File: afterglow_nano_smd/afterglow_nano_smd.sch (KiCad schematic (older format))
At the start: 106 parts, among them J1 J137_IN_C, J2 J133_IN_R, J3 Conn_Power, J4 J133_OUT_R, J5 J137_OUT_C, J6 J134_OUT_R, J7 J138_OUT_C, J8 J135_OUT_R, J9 136_OUT_C, Q1 IRF5305, Q10 IRL2905, Q11 IRL2905, Q12 IRL2905, Q13 IRL2905, Q14 IRL2905, Q15 IRL2905, Q16 IRL2905, Q2 IRF5305, Q3 IRF5305, Q4 IRF5305, Q5 IRF5305, Q6 IRF5305, Q7 IRF5305, Q8 IRF5305, Q9 IRL2905, SW1 CFG, U1 74LS165, U2 74LS165, U3 5V_Regulator, U4 arduino_nano, U5 74HC595, U6 74HC595, U7 ULN2803A

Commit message: Converting...
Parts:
- removed D2: LED, LEDs:LED_0805_HandSoldering, symbol LED
- removed R26: 220, Resistors_SMD:R_0805_HandSoldering, symbol R
- removed SW1: CFG, Buttons_Switches_THT:SW_DIP_x4_W7.62mm_Slide, symbol SW_DIP_x04
- removed U4: arduino_nano, arduino_nano:arduino_mini, symbol arduino_nano
- added A1: Arduino_Nano_v3.x, Module:Arduino_Nano, symbol MCU_Module:Arduino_Nano_v3.x
- C1: symbol CP -> Device:CP
- C2, C3: symbol C_Small -> Device:C_Small
- C4: symbol C_Small -> afterglow_nano_smd-rescue:C_Small
- D1: symbol D -> Device:D
- F1: symbol Fuse -> Device:Fuse
- J1, J2, J4, J5, J6, J7, J8: symbol Conn_01x09_Male -> Connector:Conn_01x09_Male
- J3: symbol Conn_01x02 -> afterglow_nano_smd-rescue:Conn_01x02
- J9: symbol Conn_01x03_Male -> Connector:Conn_01x03_Male
- Q1, Q2, Q3, Q4, Q5, Q6, Q7, Q8: symbol IRF9540N -> afterglow_nano_smd-rescue:IRF9540N
- Q10, Q11, Q12, Q13, Q14, Q15, Q16, Q9: symbol IRF540N -> afterglow_nano_smd-rescue:IRF540N
- R1, R10, R11, R12, R13, R14, R15, R16, R18, R19, R2, R20, R21, R22, R23, R24, R27, R28, R29, R3, R30, R31, R32, R35, R36, R37, R38, R39, R4, R5, R6, R7, R8, R9: symbol R -> Device:R
- R17, R25, R33, R34, R40, R41, R42, R43, R44, R45, R46, R47, R48, R49, R50, R51, R52, R53, R54, R55, R56, R57, R58, R59, R60, R61, R62, R63, R64, R65, R66: symbol R -> afterglow_nano_smd-rescue:R
- U1, U2: symbol 74LS165 -> 74xx:74LS165
- U3: symbol LM7805_TO220 -> Regulator_Linear:LM7805_TO220
- U5, U6: symbol 74HC595 -> 74xx:74HC595
- U7: symbol ULN2803A -> Transistor_Array:ULN2803A
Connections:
- wire segments 218 -> 242
- no-connect marks 27 -> 31

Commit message: SMD version 1.3 preparations
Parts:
- removed R33, R34: 560, Resistors_SMD:R_0805_HandSoldering, symbol afterglow_nano_smd-rescue:R
- added JP1: Jumper, Pin_Headers:Pin_Header_Straight_1x02_Pitch2.54mm, symbol Device:Jumper
- added R26: 0.22, Resistors_SMD:R_0805_HandSoldering, symbol Device:R
- added R33, R34: 10k, Resistors_SMD:R_0805_HandSoldering, symbol Device:R
- added TP1, TP2, TP3: TestPoint, symbol Connector:TestPoint
- C4: symbol afterglow_nano_smd-rescue:C_Small -> Device:C_Small
- J1, J5, J7: footprint afterglow:Molex_KK-41791-9_9x3.96mm_Straight -> Connectors_Molex:Molex_KK-41791-9_9x3.96mm_Straight
- J3: symbol afterglow_nano_smd-rescue:Conn_01x02 -> Connector:Conn_01x02_Male
- Q1, Q2, Q3, Q4, Q5, Q6, Q7, Q8: symbol afterglow_nano_smd-rescue:IRF9540N -> Transistor_FET:IRF9540N
- Q10, Q11, Q12, Q13, Q14, Q15, Q16, Q9: symbol afterglow_nano_smd-rescue:IRF540N -> Transistor_FET:IRF540N
- R1, R2, R3, R4, R5, R6, R7, R8: value 390 -> 330
- R17, R25, R40, R41, R42, R43, R44, R45, R46, R47, R48, R49, R50, R51, R52, R53, R54, R55, R56, R57, R58, R59, R60, R61, R62, R63, R64, R65, R66: symbol afterglow_nano_smd-rescue:R -> Device:R
- R27, R28, R29, R30, R31, R32: value 560 -> 10k
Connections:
- net labels added: ROW_GND
- wire segments 242 -> 257
- no-connect marks 31 -> 30
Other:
- moved on the sheet: R10, R11, R12, R13, R14, R15, R16, R9, U2, U5, U6, U7

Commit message: FW upload preparations
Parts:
- R26: footprint Resistors_SMD:R_0805_HandSoldering -> Resistors_SMD:R_2512_HandSoldering
- TP1, TP2, TP3: footprint (none) -> Pin_Headers:Pin_Header_Straight_1x01_Pitch2.54mm
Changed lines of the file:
@@
 F 0 "R26" V 6100 1100 50  0000 C CNN
 F 1 "0.22" V 6200 1100 50  0000 C CNN
-F 2 "Resistors_SMD:R_0805_HandSoldering" V 6130 1100 50  0001 C CNN
+F 2 "Resistors_SMD:R_2512_HandSoldering" V 6130 1100 50  0001 C CNN
 F 3 "" H 6200 1100 50  0001 C CNN
 	1    6200 1100
@@
 F 0 "TP1" H 5758 3320 50  0000 L CNN
 F 1 "TestPoint" H 5758 3229 50  0000 L CNN
-F 2 "" H 5900 3200 50  0001 C CNN
+F 2 "Pin_Headers:Pin_Header_Straight_1x01_Pitch2.54mm" H 5900 3200 50  0001 C CNN
 F 3 "~" H 5900 3200 50  0001 C CNN
 	1    5700 3200
@@
 F 0 "TP2" H 6408 3320 50  0000 L CNN
 F 1 "TestPoint" H 6408 3229 50  0000 L CNN
-F 2 "" H 6550 3200 50  0001 C CNN
+F 2 "Pin_Headers:Pin_Header_Straight_1x01_Pitch2.54mm" H 6550 3200 50  0001 C CNN
 F 3 "~" H 6550 3200 50  0001 C CNN
 	1    6350 3200
@@
 F 0 "TP3" H 7058 3320 50  0000 L CNN
 F 1 "TestPoint" H 7058 3229 50  0000 L CNN
-F 2 "" H 7200 3200 50  0001 C CNN
+F 2 "Pin_Headers:Pin_Header_Straight_1x01_Pitch2.54mm" H 7200 3200 50  0001 C CNN
 F 3 "~" H 7200 3200 50  0001 C CNN
 	1    7000 3200

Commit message: v1.3 PCB progress
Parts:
- A1: footprint Module:Arduino_Nano -> Modules:Arduino_Nano
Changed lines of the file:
@@
 L Connector:Conn_01x02_Male J3
 U 1 1 59DA2DDC
-P 950 1100
-F 0 "J3" H 950 1200 50  0000 C CNN
-F 1 "Conn_Power" H 950 900 50  0000 C CNN
-F 2 "Connectors_Molex:Molex_KK-41791-02_02x3.96mm_Straight" H 950 1100 50  0001 C CNN
-F 3 "" H 950 1100 50  0001 C CNN
-	1    950  1100
-	1    0    0    1
+P 950 1000
+F 0 "J3" H 950 1100 50  0000 C CNN
+F 1 "Conn_Power" H 950 800 50  0000 C CNN
+F 2 "Connectors_Molex:Molex_KK-41791-02_02x3.96mm_Straight" H 950 1000 50  0001 C CNN
+F 3 "" H 950 1000 50  0001 C CNN
+	1    950  1000
+	1    0    0    -1
 $EndComp
 NoConn ~ 900  2550
@@
 F 0 "A1" H 3850 1250 50  0000 C CNN
 F 1 "Arduino_Nano_v3.x" H 3850 1150 50  0000 C CNN
-F 2 "Module:Arduino_Nano" H 4500 1400 50  0001 L CNN
+F 2 "Modules:Arduino_Nano" H 4500 1400 50  0001 L CNN
 F 3 "http://www.mouser.com/pdfdocs/Gravitech_Arduino_Nano3_0.pdf" H 4350 1350 50  0001 C CNN
 	1    4350 2350

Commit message: v1.3 progressing
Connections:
- net labels added: SUP_GND
- net labels removed: ROW_GND
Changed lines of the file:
@@
 Connection ~ 6000 1100
 Text Label 6000 950  0    60   ~ 0
-ROW_GND
+SUP_GND
 Wire Wire Line
 	10300 1050 10300 1150
@@
 Connection ~ 10300 6300
 Text Label 10300 1900 0    60   ~ 0
-ROW_GND
+SUP_GND
 Text Label 10300 2650 0    60   ~ 0
-ROW_GND
+SUP_GND
 Text Label 10300 3400 0    60   ~ 0
-ROW_GND
+SUP_GND
 Text Label 10300 4150 0    60   ~ 0
-ROW_GND
+SUP_GND
 Text Label 10300 4900 0    60   ~ 0
-ROW_GND
+SUP_GND
 Text Label 10300 5650 0    60   ~ 0
-ROW_GND
+SUP_GND
 Text Label 10300 6400 0    60   ~ 0
-ROW_GND
+SUP_GND
 Text Label 10300 1150 0    60   ~ 0
-ROW_GND
+SUP_GND
 Wire Wire Line
 	6000 1100 6000 2350
@@
 Connection ~ 8200 1050
 $Comp
-L power:GND #PWR03
-U 1 1 5BA996DF
-P 7900 1050
-F 0 "#PWR03" H 7900 800 50  0001 C CNN
-F 1 "GND" H 7905 877 50  0000 C CNN
-F 2 "" H 7900 1050 50  0001 C CNN
-F 3 "" H 7900 1050 50  0001 C CNN
-	1    7900 1050
-	1    0    0    -1
-$EndComp
-$Comp
 L Device:R R28
 U 1 1 5BA99EBD
@@
 Connection ~ 8200 3300
 $Comp
-L power:GND #PWR04
-U 1 1 5BA9A69A
-P 7900 1800
-F 0 "#PWR04" H 7900 1550 50  0001 C CNN
-F 1 "GND" H 7905 1627 50  0000 C CNN
-F 2 "" H 7900 1800 50  0001 C CNN
-F 3 "" H 7900 1800 50  0001 C CNN
-	1    7900 1800
-	1    0    0    -1
-$EndComp
-$Comp
-L power:GND #PWR05
-U 1 1 5BA9A77D
-P 7900 2550
-F 0 "#PWR05" H 7900 2300 50  0001 C CNN
-F 1 "GND" H 7905 2377 50  0000 C CNN
-F 2 "" H 7900 2550 50  0001 C CNN
-F 3 "" H 7900 2550 50  0001 C CNN
-	1    7900 2550
-	1    0    0    -1
-$EndComp
-$Comp
-L power:GND #PWR06
-U 1 1 5BA9AA10
-P 7900 3300
-F 0 "#PWR06" H 7900 3050 50  0001 C CNN
-F 1 "GND" H 7905 3127 50  0000 C CNN
-F 2 "" H 7900 3300 50  0001 C CNN
-F 3 "" H 7900 3300 50  0001 C CNN
-	1    7900 3300
-	1    0    0    -1
-$EndComp
-$Comp
 L Device:R R31
 U 1 1 5BA9ADD5
@@
 Connection ~ 8200 4050
 $Comp
-L power:GND #PWR07
-U 1 1 5BA9AEEF
-P 7900 4050
-F 0 "#PWR07" H 7900 3800 50  0001 C CNN
-F 1 "GND" H 7905 3877 50  0000 C CNN
-F 2 "" H 7900 4050 50  0001 C CNN
-F 3 "" H 7900 4050 50  0001 C CNN
-	1    7900 4050
-	1    0    0    -1
-$EndComp
-$Comp
 L Device:R R32
 U 1 1 5BA9B262
@@
 Connection ~ 8250 6300
 $Comp
-L power:GND #PWR08
-U 1 1 5BA9BE49
-P 7900 4800
-F 0 "#PWR08" H 7900 4550 50  0001 C CNN
-F 1 "GND" H 7905 4627 50  0000 C CNN
-F 2 "" H 7900 4800 50  0001 C CNN
-F 3 "" H 7900 4800 50  0001 C CNN
-	1    7900 4800
-	1    0    0    -1
-$EndComp
-$Comp
-L power:GND #PWR09
-U 1 1 5BA9C1D4
-P 7900 5550
-F 0 "#PWR09" H 7900 5300 50  0001 C CNN
-F 1 "GND" H 7905 5377 50  0000 C CNN
-F 2 "" H 7900 5550 50  0001 C CNN
-F 3 "" H 7900 5550 50  0001 C CNN
-	1    7900 5550
-	1    0    0    -1
-$EndComp
-$Comp
-L power:GND #PWR011
-U 1 1 5BA9C39F
-P 7950 6300
-F 0 "#PWR011" H 7950 6050 50  0001 C CNN
-F 1 "GND" H 7955 6127 50  0000 C CNN
-F 2 "" H 7950 6300 50  0001 C CNN
-F 3 "" H 7950 6300 50  0001 C CNN
-	1    7950 6300
-	1    0    0    -1
-$EndComp
-$Comp
 L Device:Jumper JP1
 U 1 1 5BAB0DAE
@@
 Text Label 7000 3200 2    60   ~ 0
 18V
+Text Label 7900 1050 2    60   ~ 0
+SUP_GND
+Text Label 7900 1800 2    60   ~ 0
+SUP_GND
+Text Label 7900 2550 2    60   ~ 0
+SUP_GND
+Text Label 7900 3300 2    60   ~ 0
+SUP_GND
+Text Label 7900 4050 2    60   ~ 0
+SUP_GND
+Text Label 7900 4800 2    60   ~ 0
+SUP_GND
+Text Label 7900 5550 2    60   ~ 0
+SUP_GND
+Text Label 7950 6300 2    60   ~ 0
+SUP_GND
 $EndSCHEMATC

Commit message: Added the configuration DIP switch back - it might be handy after all
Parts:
- removed JP1: Jumper, Pin_Headers:Pin_Header_Straight_1x02_Pitch2.54mm, symbol Device:Jumper
- added SW1: CFG, Buttons_Switches_THT:SW_DIP_x4_W7.62mm_Slide, symbol Switch:SW_DIP_x04
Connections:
- wire segments 257 -> 265
- no-connect marks 30 -> 27
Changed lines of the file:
@@
 Wire Wire Line
 	4550 1350 4550 1250
-NoConn ~ 3850 2550
-NoConn ~ 3850 2650
 NoConn ~ 4850 2150
-NoConn ~ 3850 2850
 NoConn ~ 3850 2950
 NoConn ~ 3850 3050
@@
 $EndComp
 Connection ~ 8250 6300
-$Comp
-L Device:Jumper JP1
-U 1 1 5BAB0DAE
-P 3550 2750
-F 0 "JP1" H 3550 2650 50  0000 C CNN
-F 1 "Jumper" H 3550 2550 50  0000 C CNN
-F 2 "Pin_Headers:Pin_Header_Straight_1x02_Pitch2.54mm" H 3550 2750 50  0001 C CNN
-F 3 "~" H 3550 2750 50  0001 C CNN
-	1    3550 2750
-	1    0    0    -1
-$EndComp
-$Comp
-L power:GND #PWR02
-U 1 1 5BAB10AE
-P 3250 2750
-F 0 "#PWR02" H 3250 2500 50  0001 C CNN
-F 1 "GND" H 3255 2577 50  0000 C CNN
-F 2 "" H 3250 2750 50  0001 C CNN
-F 3 "" H 3250 2750 50  0001 C CNN
-	1    3250 2750
-	1    0    0    -1
-$EndComp
 Wire Wire Line
 	4250 5600 4350 5600
@@
 Text Label 7950 6300 2    60   ~ 0
 SUP_GND
+$Comp
+L Switch:SW_DIP_x04 SW1
+U 1 1 5BB93746
+P 3550 2750
+F 0 "SW1" H 3550 3217 50  0000 C CNN
+F 1 "CFG" H 3550 2450 50  0000 C CNN
+F 2 "Buttons_Switches_THT:SW_DIP_x4_W7.62mm_Slide" H 3550 2750 50  0001 C CNN
+F 3 "" H 3550 2750 50  0001 C CNN
+	1    3550 2750
+	1    0    0    -1
+$EndComp
+Wire Wire Line
+	3250 2550 3100 2550
+Wire Wire Line
+	3100 2550 3100 2650
+Wire Wire Line
+	3250 2650 3100 2650
+Connection ~ 3100 2650
+Wire Wire Line
+	3100 2650 3100 2750
+Wire Wire Line
+	3250 2750 3100 2750
+Connection ~ 3100 2750
+Wire Wire Line
+	3100 2750 3100 2850
+Wire Wire Line
+	3250 2850 3100 2850
+Connection ~ 3100 2850
+Wire Wire Line
+	3100 2850 3100 3100
+$Comp
+L power:GND #PWR0106
+U 1 1 5BBDA8BB
+P 3100 3100
+F 0 "#PWR0106" H 3100 2850 50  0001 C CNN
+F 1 "GND" H 3105 2927 50  0000 C CNN
+F 2 "" H 3100 3100 50  0001 C CNN
+F 3 "" H 3100 3100 50  0001 C CNN
+	1    3100 3100
+	1    0    0    -1
+$EndComp
 $EndSCHEMATC

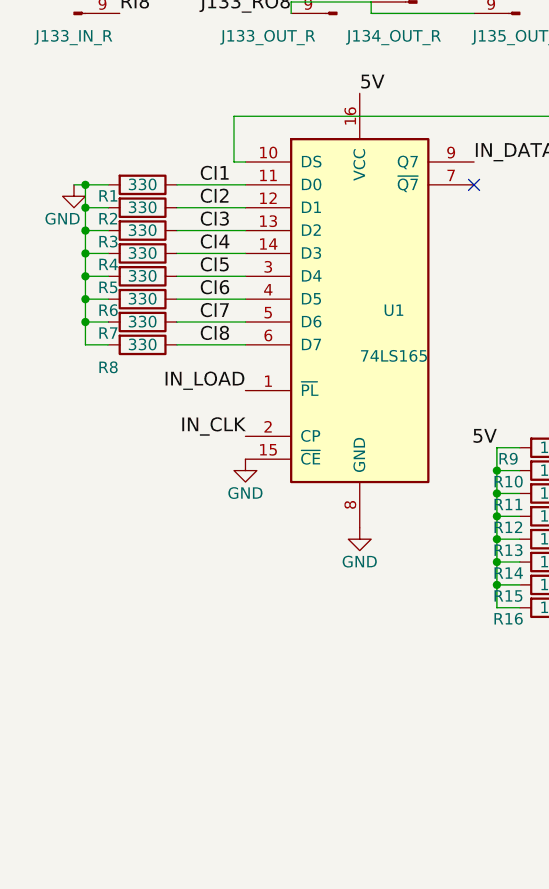
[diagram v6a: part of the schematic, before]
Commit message: Added input Zener diodes
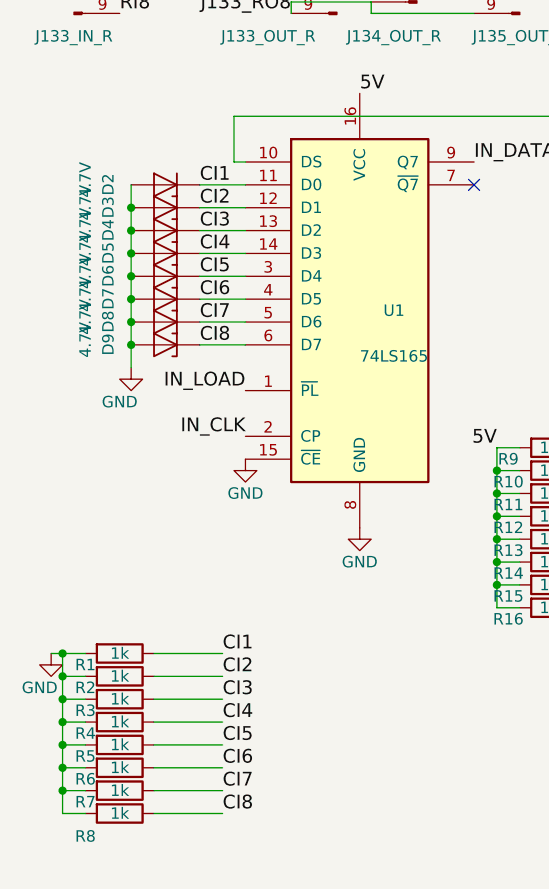
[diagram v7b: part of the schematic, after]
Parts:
- added D2, D3, D4, D5, D6, D7, D8, D9: 4.7V, Diodes_SMD:D_SOD-323_HandSoldering, symbol Device:D_Zener
- R1, R2, R3, R4, R5, R6, R7, R8: value 330 -> 1k
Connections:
- net CI1: now also D2.1 (K)
- net CI2: now also D3.1 (K)
- net CI3: now also D4.1 (K)
- net CI4: now also D5.1 (K)
- net CI5: now also D6.1 (K)
- net CI6: now also D7.1 (K)
- net CI7: now also D8.1 (K)
- net CI8: now also D9.1 (K)
- net GND: now also D2.2 (A), D3.2 (A), D4.2 (A), D5.2 (A), D6.2 (A), D7.2 (A), D8.2 (A), D9.2 (A)
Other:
- moved on the sheet: R1, R2, R3, R4, R5, R6, R7, R8

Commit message: Minor schematic updates
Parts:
- Q1, Q2, Q3, Q4, Q5, Q6, Q7, Q8: value IRF5305 -> IRFR9024
- Q10, Q11, Q12, Q13, Q14, Q15, Q16, Q9: value IRL2905 -> IRLR024
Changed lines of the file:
@@
 P 8100 850
 F 0 "Q1" H 8350 925 50  0000 L CNN
-F 1 "IRF5305" H 8350 850 50  0000 L CNN
+F 1 "IRFR9024" H 8350 850 50  0000 L CNN
 F 2 "TO_SOT_Packages_SMD:TO-252-2" H 8350 775 50  0001 L CIN
 F 3 "" H 8100 850 50  0001 L CNN
@@
 P 8100 1600
 F 0 "Q2" H 8350 1675 50  0000 L CNN
-F 1 "IRF5305" H 8350 1600 50  0000 L CNN
+F 1 "IRFR9024" H 8350 1600 50  0000 L CNN
 F 2 "TO_SOT_Packages_SMD:TO-252-2" H 8350 1525 50  0001 L CIN
 F 3 "" H 8100 1600 50  0001 L CNN
@@
 P 8100 2350
 F 0 "Q3" H 8350 2425 50  0000 L CNN
-F 1 "IRF5305" H 8350 2350 50  0000 L CNN
+F 1 "IRFR9024" H 8350 2350 50  0000 L CNN
 F 2 "TO_SOT_Packages_SMD:TO-252-2" H 8350 2275 50  0001 L CIN
 F 3 "" H 8100 2350 50  0001 L CNN
@@
 P 8100 3100
 F 0 "Q4" H 8350 3175 50  0000 L CNN
-F 1 "IRF5305" H 8350 3100 50  0000 L CNN
+F 1 "IRFR9024" H 8350 3100 50  0000 L CNN
 F 2 "TO_SOT_Packages_SMD:TO-252-2" H 8350 3025 50  0001 L CIN
 F 3 "" H 8100 3100 50  0001 L CNN
@@
 P 8100 3850
 F 0 "Q5" H 8350 3925 50  0000 L CNN
-F 1 "IRF5305" H 8350 3850 50  0000 L CNN
+F 1 "IRFR9024" H 8350 3850 50  0000 L CNN
 F 2 "TO_SOT_Packages_SMD:TO-252-2" H 8350 3775 50  0001 L CIN
 F 3 "" H 8100 3850 50  0001 L CNN
@@
 P 8100 4600
 F 0 "Q6" H 8350 4675 50  0000 L CNN
-F 1 "IRF5305" H 8350 4600 50  0000 L CNN
+F 1 "IRFR9024" H 8350 4600 50  0000 L CNN
 F 2 "TO_SOT_Packages_SMD:TO-252-2" H 8350 4525 50  0001 L CIN
 F 3 "" H 8100 4600 50  0001 L CNN
@@
 P 8100 5350
 F 0 "Q7" H 8350 5425 50  0000 L CNN
-F 1 "IRF5305" H 8350 5350 50  0000 L CNN
+F 1 "IRFR9024" H 8350 5350 50  0000 L CNN
 F 2 "TO_SOT_Packages_SMD:TO-252-2" H 8350 5275 50  0001 L CIN
 F 3 "" H 8100 5350 50  0001 L CNN
@@
 P 8150 6100
 F 0 "Q8" H 8400 6175 50  0000 L CNN
-F 1 "IRF5305" H 8400 6100 50  0000 L CNN
+F 1 "IRFR9024" H 8400 6100 50  0000 L CNN
 F 2 "TO_SOT_Packages_SMD:TO-252-2" H 8400 6025 50  0001 L CIN
 F 3 "" H 8150 6100 50  0001 L CNN
@@
 P 10200 850
 F 0 "Q9" H 10450 850 50  0000 L CNN
-F 1 "IRL2905" H 10450 750 50  0000 L CNN
+F 1 "IRLR024" H 10450 750 50  0000 L CNN
 F 2 "TO_SOT_Packages_SMD:TO-252-2" H 10450 775 50  0001 L CIN
 F 3 "" H 10200 850 50  0001 L CNN
@@
 P 10200 1600
 F 0 "Q10" H 10450 1600 50  0000 L CNN
-F 1 "IRL2905" H 10450 1500 50  0000 L CNN
+F 1 "IRLR024" H 10450 1500 50  0000 L CNN
 F 2 "TO_SOT_Packages_SMD:TO-252-2" H 10450 1525 50  0001 L CIN
 F 3 "" H 10200 1600 50  0001 L CNN
@@
 P 10200 2350
 F 0 "Q11" H 10450 2350 50  0000 L CNN
-F 1 "IRL2905" H 10450 2250 50  0000 L CNN
+F 1 "IRLR024" H 10450 2250 50  0000 L CNN
 F 2 "TO_SOT_Packages_SMD:TO-252-2" H 10450 2275 50  0001 L CIN
 F 3 "" H 10200 2350 50  0001 L CNN
@@
 P 10200 3100
 F 0 "Q12" H 10450 3100 50  0000 L CNN
-F 1 "IRL2905" H 10450 3000 50  0000 L CNN
+F 1 "IRLR024" H 10450 3000 50  0000 L CNN
 F 2 "TO_SOT_Packages_SMD:TO-252-2" H 10450 3025 50  0001 L CIN
 F 3 "" H 10200 3100 50  0001 L CNN
@@
 P 10200 3850
 F 0 "Q13" H 10450 3850 50  0000 L CNN
-F 1 "IRL2905" H 10450 3750 50  0000 L CNN
+F 1 "IRLR024" H 10450 3750 50  0000 L CNN
 F 2 "TO_SOT_Packages_SMD:TO-252-2" H 10450 3775 50  0001 L CIN
 F 3 "" H 10200 3850 50  0001 L CNN
@@
 P 10200 4600
 F 0 "Q14" H 10450 4600 50  0000 L CNN
-F 1 "IRL2905" H 10450 4500 50  0000 L CNN
+F 1 "IRLR024" H 10450 4500 50  0000 L CNN
 F 2 "TO_SOT_Packages_SMD:TO-252-2" H 10450 4525 50  0001 L CIN
 F 3 "" H 10200 4600 50  0001 L CNN
@@
 P 10200 5350
 F 0 "Q15" H 10450 5350 50  0000 L CNN
-F 1 "IRL2905" H 10450 5250 50  0000 L CNN
+F 1 "IRLR024" H 10450 5250 50  0000 L CNN
 F 2 "TO_SOT_Packages_SMD:TO-252-2" H 10450 5275 50  0001 L CIN
 F 3 "" H 10200 5350 50  0001 L CNN
@@
 P 10200 6100
 F 0 "Q16" H 10450 6100 50  0000 L CNN
-F 1 "IRL2905" H 10450 6000 50  0000 L CNN
+F 1 "IRLR024" H 10450 6000 50  0000 L CNN
 F 2 "TO_SOT_Packages_SMD:TO-252-2" H 10450 6025 50  0001 L CIN
 F 3 "" H 10200 6100 50  0001 L CNN
